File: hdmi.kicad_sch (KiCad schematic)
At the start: 26 parts, among them U14 NTS0102_XSON, U15 PI3HDX511DZLE, U18 74LVC1T45GM

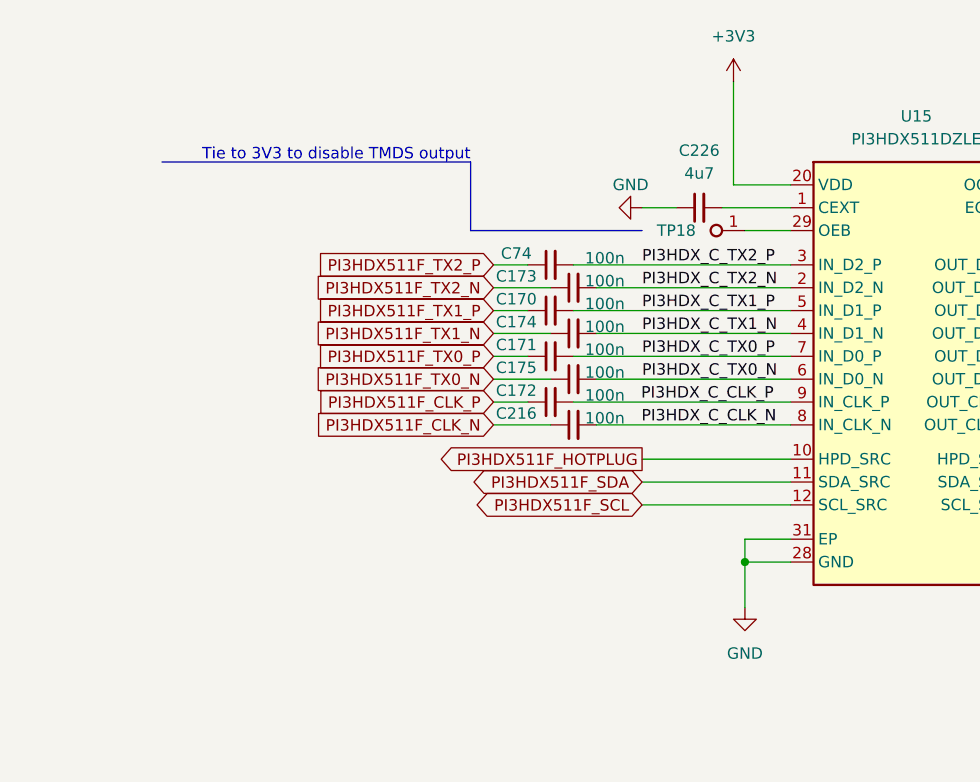
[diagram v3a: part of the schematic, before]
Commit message: [#56264] Add 4x100nF array and more GND via
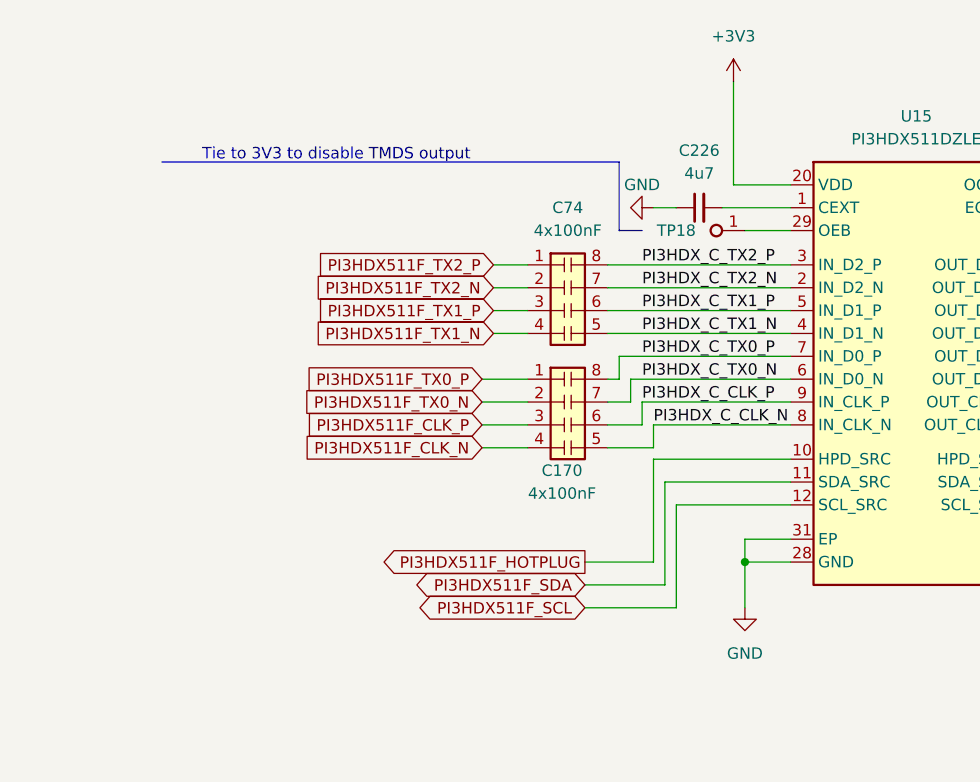
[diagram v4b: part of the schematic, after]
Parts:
- removed C170, C171, C172, C173, C174, C175, C216, C74: C_100n_0402, antmicro-footprints:C_0402_1005Metric, symbol antmicroCapacitors0402:C_100n_0402
- added C170, C74: C_4x100nF_0508_1220Metric_array, antmicro-footprints:C_Array_0508_1220Metric, symbol antmicroCapacitorsmisc:C_4x100nF_0508_1220Metric_array
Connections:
- net PI3HDX511F_CLK_N: now also C170.4 (R4.1)
- net PI3HDX511F_CLK_P: now also C170.3 (R3.1)
- net PI3HDX511F_TX0_N: now also C170.2 (R2.1)
- net PI3HDX511F_TX0_P: now also C170.1 (R1.1)
- net PI3HDX511F_TX1_N: now also C74.4 (R4.1)
- net PI3HDX511F_TX1_P: now also C74.3 (R3.1)
- net PI3HDX511F_TX2_N: now also C74.2 (R2.1)
- net PI3HDX511F_TX2_P: now also C74.1 (R1.1)
- net PI3HDX_C_CLK_N: now also C170.5 (R4.2)
- net PI3HDX_C_CLK_P: now also C170.6 (R3.2)
- net PI3HDX_C_TX0_N: now also C170.7 (R2.2)
- net PI3HDX_C_TX0_P: now also C170.8 (R1.2)
- net PI3HDX_C_TX1_N: now also C74.5 (R4.2)
- net PI3HDX_C_TX1_P: now also C74.6 (R3.2)
- net PI3HDX_C_TX2_N: now also C74.7 (R2.2)
- net PI3HDX_C_TX2_P: now also C74.8 (R1.2)

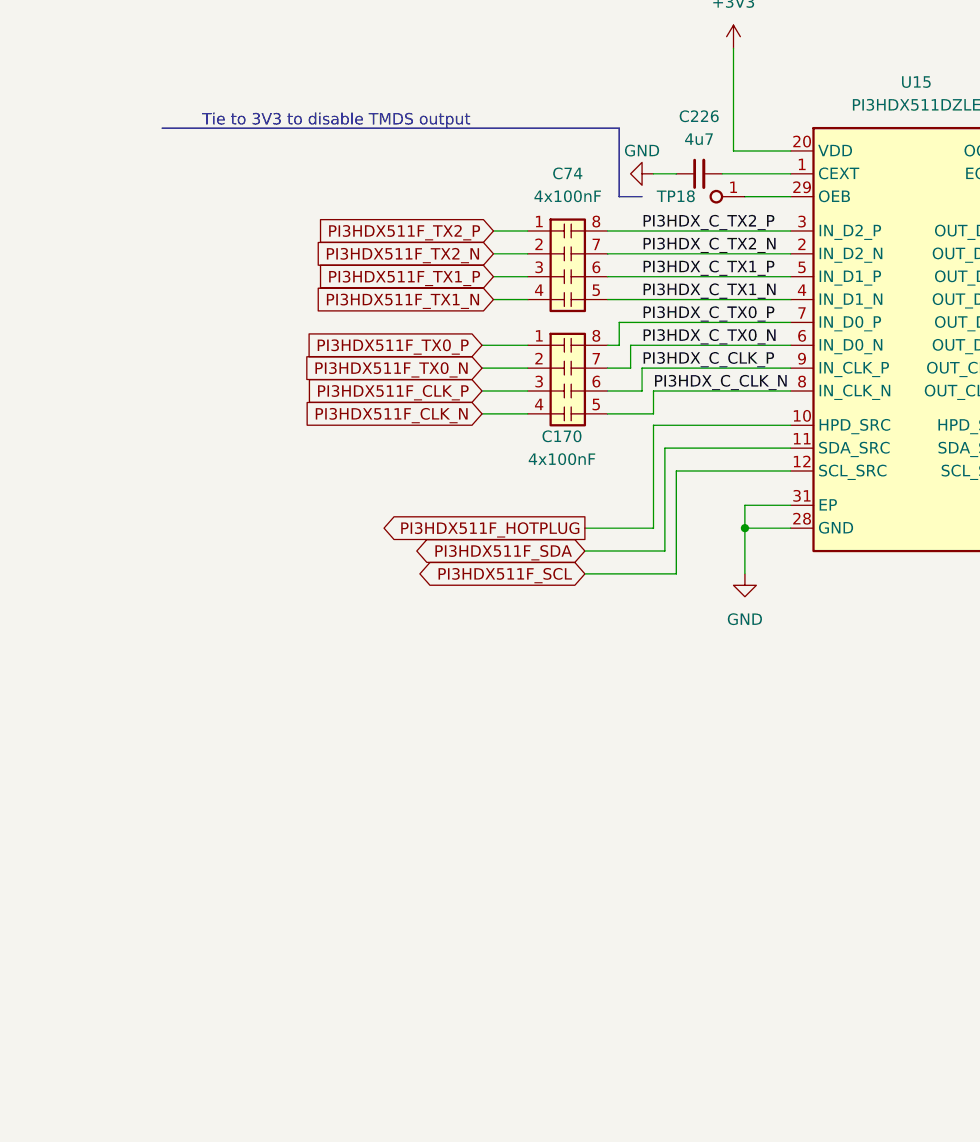
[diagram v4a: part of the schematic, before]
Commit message: Place cap arrays. Route PCIe. Start routing HDMI
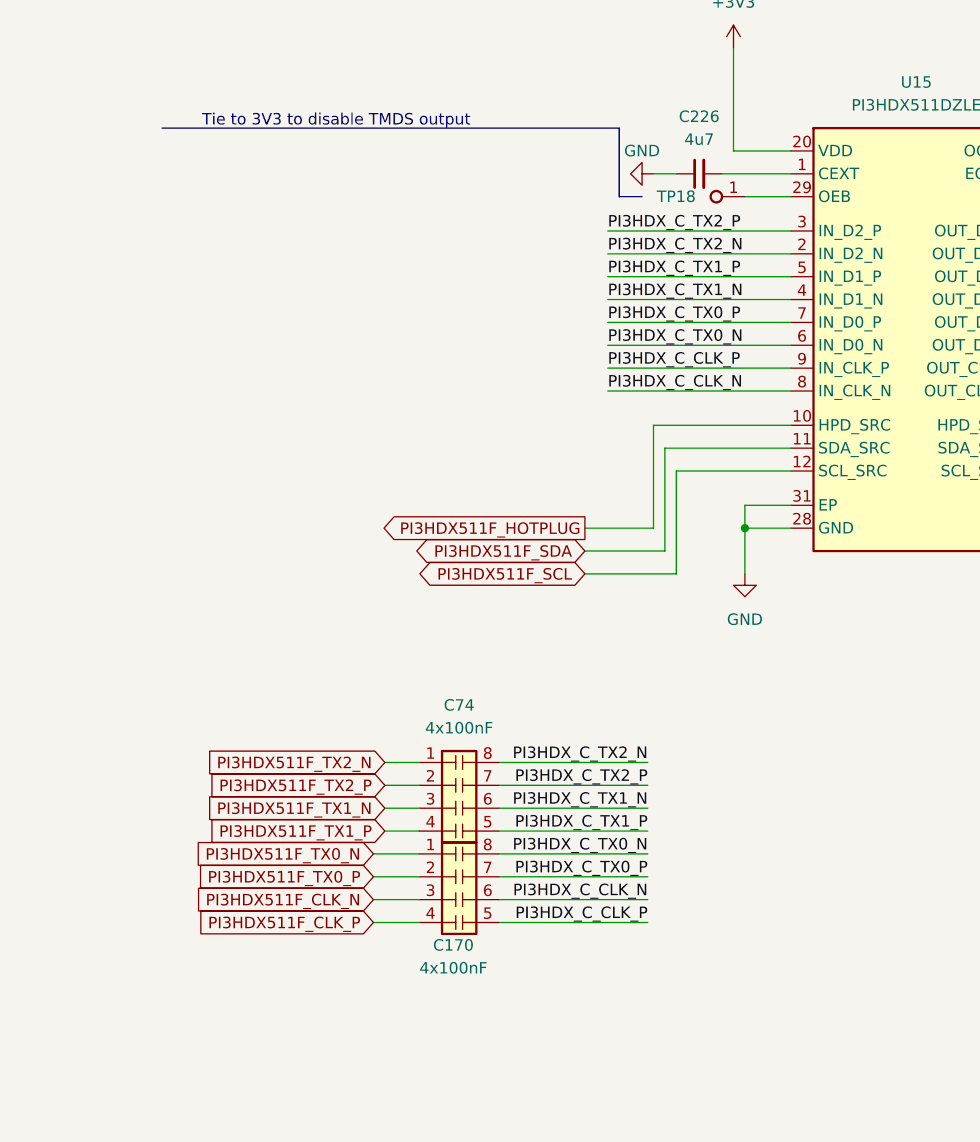
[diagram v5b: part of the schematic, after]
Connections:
- net PI3HDX511F_CLK_N: now also C170.3 (R3.1); no longer C170.4 (R4.1)
- net PI3HDX511F_CLK_P: now also C170.4 (R4.1); no longer C170.3 (R3.1)
- net PI3HDX511F_TX0_N: now also C170.1 (R1.1); no longer C170.2 (R2.1)
- net PI3HDX511F_TX0_P: now also C170.2 (R2.1); no longer C170.1 (R1.1)
- net PI3HDX511F_TX1_N: now also C74.3 (R3.1); no longer C74.4 (R4.1)
- net PI3HDX511F_TX1_P: now also C74.4 (R4.1); no longer C74.3 (R3.1)
- net PI3HDX511F_TX2_N: now also C74.1 (R1.1); no longer C74.2 (R2.1)
- net PI3HDX511F_TX2_P: now also C74.2 (R2.1); no longer C74.1 (R1.1)
- net PI3HDX_C_CLK_N: now also C170.6 (R3.2); no longer C170.5 (R4.2)
- net PI3HDX_C_CLK_P: now also C170.5 (R4.2); no longer C170.6 (R3.2)
- net PI3HDX_C_TX0_N: now also C170.8 (R1.2); no longer C170.7 (R2.2)
- net PI3HDX_C_TX0_P: now also C170.7 (R2.2); no longer C170.8 (R1.2)
- net PI3HDX_C_TX1_N: now also C74.6 (R3.2); no longer C74.5 (R4.2)
- net PI3HDX_C_TX1_P: now also C74.5 (R4.2); no longer C74.6 (R3.2)
- net PI3HDX_C_TX2_N: now also C74.8 (R1.2); no longer C74.7 (R2.2)
- net PI3HDX_C_TX2_P: now also C74.7 (R2.2); no longer C74.8 (R1.2)
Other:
- moved on the sheet: C170, C74

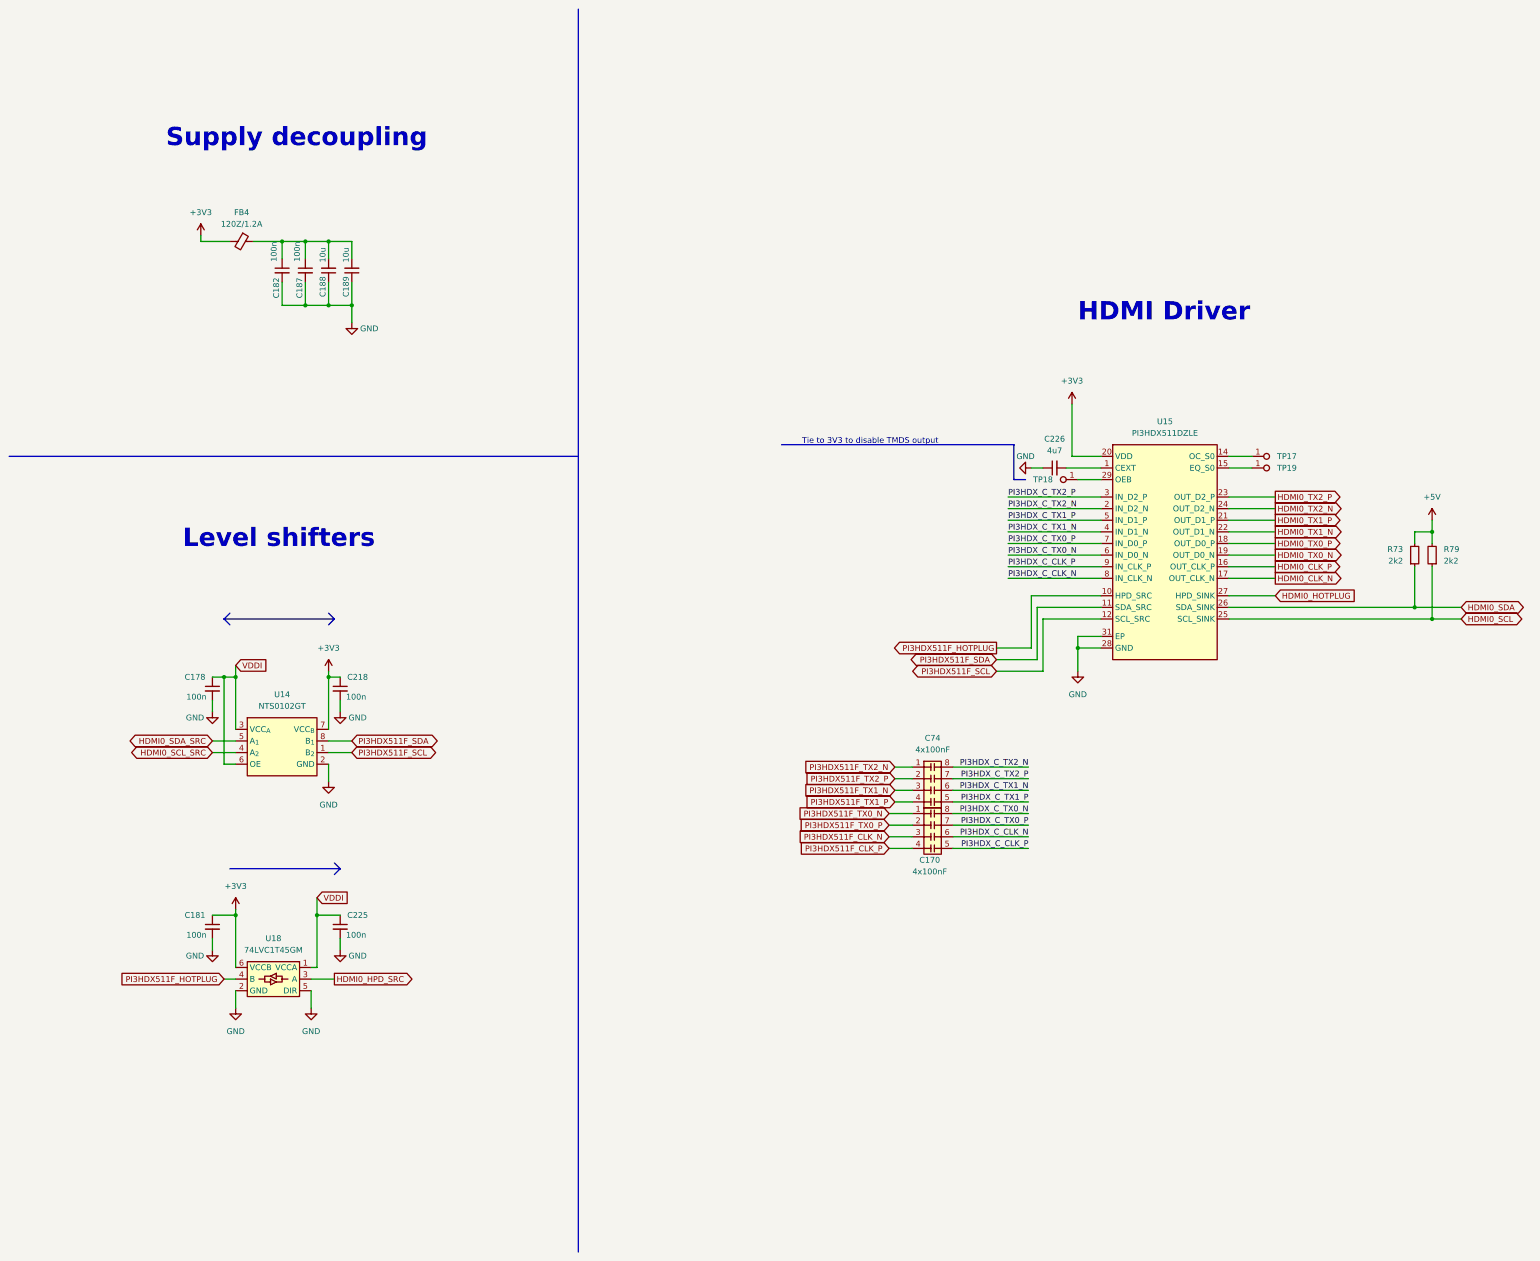
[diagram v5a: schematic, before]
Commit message: [#55992] Place left out components
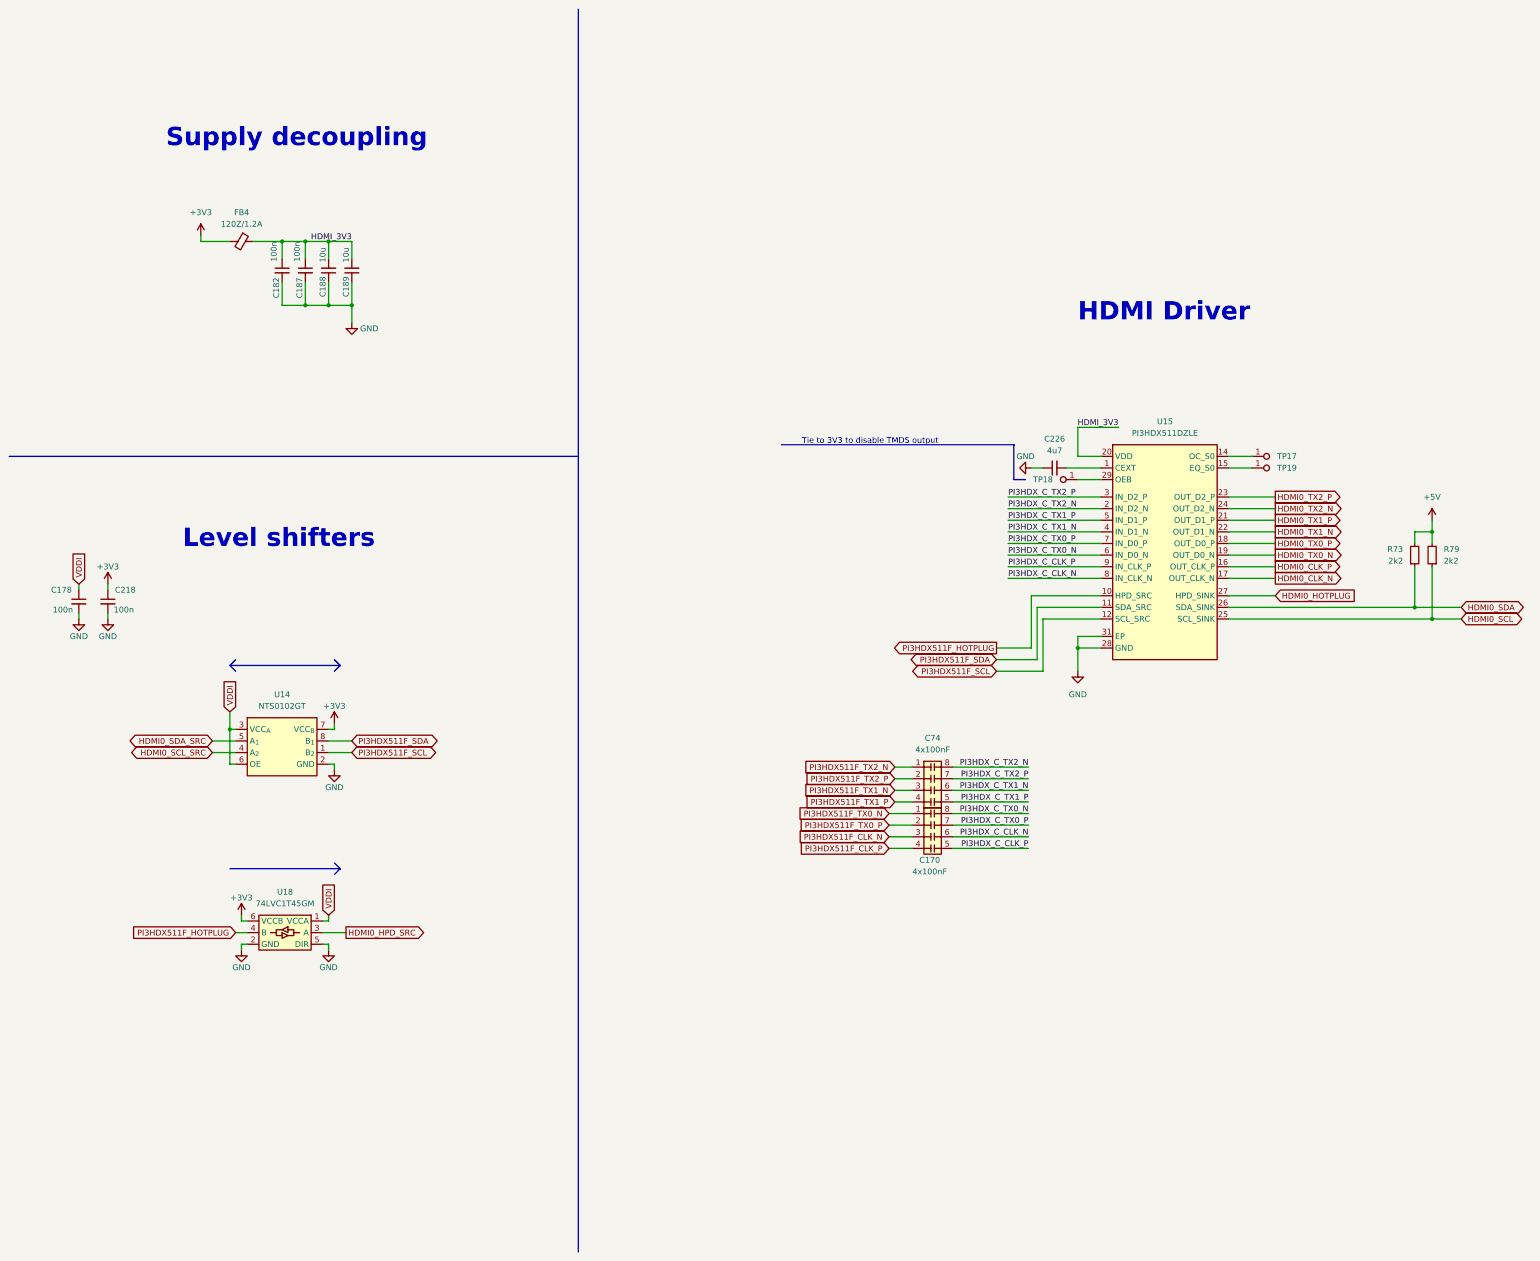
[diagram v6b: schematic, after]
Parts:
- removed C181, C225: C_100n_0402, antmicro-footprints:C_0402_1005Metric, symbol antmicroCapacitors0402:C_100n_0402
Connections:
- net +3V3: no longer U15.20 (VDD), U15.30 (VDD)
- net HDMI_3V3: now reaches C182.1, C187.1, C188.2, C189.2, FB4.1
- net HDMI_3V3: now also U15.20 (VDD), U15.30 (VDD)
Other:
- moved on the sheet: C178, C218, U18

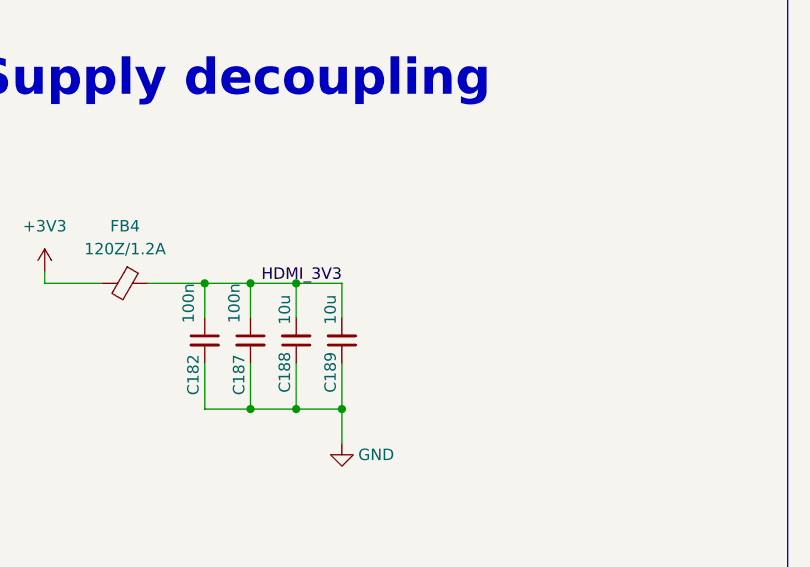
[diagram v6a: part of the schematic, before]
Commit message: [#56952] Place top designators, clean ERC
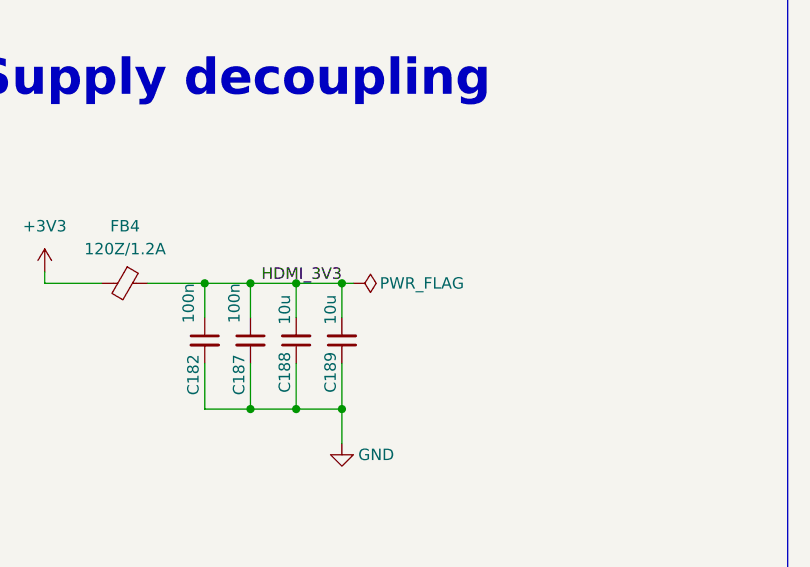
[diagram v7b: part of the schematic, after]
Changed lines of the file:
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@@
   (junction (at 72.39 63.5) (diameter 0) (color 0 0 0 0)
   )
+  (junction (at 87.63 63.5) (diameter 0) (color 0 0 0 0)
+  )
   (junction (at 60.96 170.18) (diameter 0) (color 0 0 0 0)
   )
@@
     (stroke (width 0) (type default))
   )
+  (wire (pts (xy 87.63 63.5) (xy 88.9 63.5))
+    (stroke (width 0) (type default))
+  )
   (wire (pts (xy 235.585 188.595) (xy 219.075 188.595))
     (stroke (width 0) (type default))
@@
         )
       )
+    )
+  )
+  (symbol (lib_id "antmicropower:PWR_FLAG") (at 88.9 63.5 270) (unit 1)
+    (in_bom yes) (on_board yes) (dnp no)
+    (property "Reference" "#FLG024" (at 90.805 63.5 0)
+      (effects (font (size 1.27 1.27)) hide)
+    )
+    (property "Value" "PWR_FLAG" (at 96.52 63.5 90)
+      (effects (font (size 1.27 1.27)))
+    )
+    (property "Footprint" "" (at 88.9 63.5 0)
+      (effects (font (size 1.27 1.27)) hide)
+    )
+    (property "Datasheet" "" (at 88.9 63.5 0)
+      (effects (font (size 1.27 1.27)) hide)
+    )
+    (pin "1")
+    (instances
+      (project "polarfire-som"
+        (path "/db4a0d3e-2eb3-499e-977d-6eb378cfd3ed/9d03ca8b-00f4-4bc6-89d1-f3be2c1a83b3"
+          (reference "#FLG024") (unit 1)
+        )
+      )
